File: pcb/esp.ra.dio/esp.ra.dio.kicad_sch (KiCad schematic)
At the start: 20 parts, among them J1 A, J2 B, J3 C, J4 D, J5 START, J6 SELECT, J7 JOY, J8 BATTERY, J9 NRF24L01 Connector, SW1 OPTS, SW2 POWER, U1 RP2040 Tiny, U3 MIC5205-3.0YM5

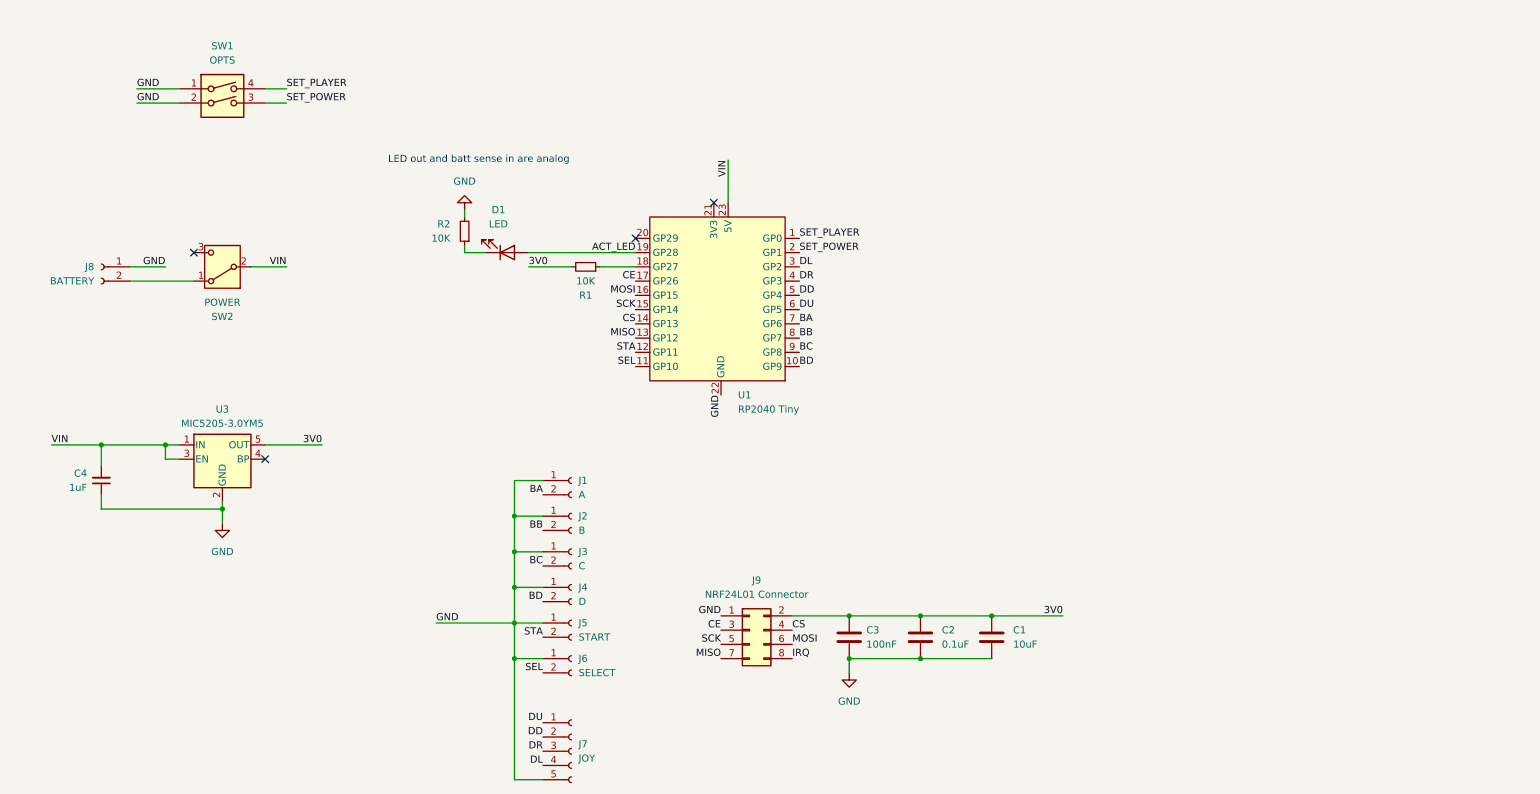
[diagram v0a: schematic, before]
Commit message: super-mini symbol/footprint
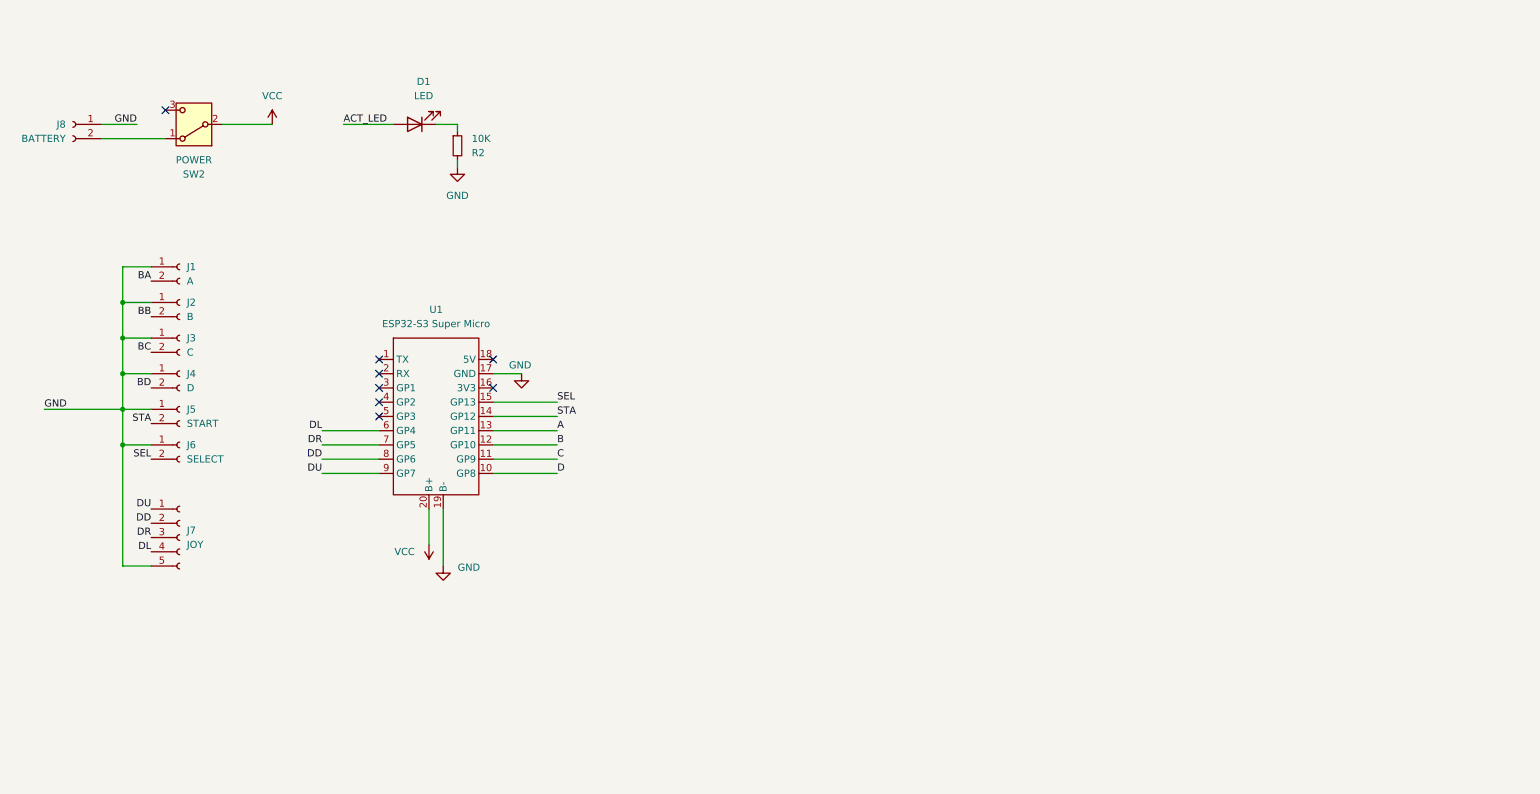
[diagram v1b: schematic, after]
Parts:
- removed C1: 10uF, Capacitor_SMD:C_0805_2012Metric_Pad1.18x1.45mm_HandSolder, symbol Device:C
- removed C2: 0.1uF, Capacitor_SMD:C_0805_2012Metric_Pad1.18x1.45mm_HandSolder, symbol Device:C
- removed C3: 100nF, Capacitor_SMD:C_0805_2012Metric_Pad1.18x1.45mm_HandSolder, symbol Device:C
- removed C4: 1uF, Capacitor_SMD:C_0805_2012Metric_Pad1.18x1.45mm_HandSolder, symbol Device:C_Small
- removed J9: NRF24L01 Connector, Connector_PinHeader_2.54mm:PinHeader_2x04_P2.54mm_Vertical, symbol Connector_Generic:Conn_02x04_Odd_Even
- removed R1: 10K, Resistor_SMD:R_0805_2012Metric_Pad1.20x1.40mm_HandSolder, symbol Device:R_Small
- removed SW1: OPTS, Button_Switch_SMD:SW_DIP_SPSTx02_Slide_6.7x6.64mm_W8.61mm_P2.54mm_LowProfile, symbol Switch:SW_DIP_x02
- removed U1: RP2040 Tiny, RP2040Zero:RP2040-Zero, symbol RP2040Zero:RP2040-Zero
- removed U3: MIC5205-3.0YM5, Package_TO_SOT_SMD:SOT-23-5, symbol Regulator_Linear:MIC5205-3.0YM5
- added U1: ESP32-S3 Super Micro, MCU_Espressif_ESP32_DevBoard:ESP32-S3-SuperMicro, symbol MCU_Espressif_ESP32_DevBoard:ESP32-S3-SuperMicro
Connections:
- net DD: now also U1.8 (GP6)
- net DL: now also U1.6 (GP4)
- net DR: now also U1.7 (GP5)
- net DU: now also U1.9 (GP7)
- net GND: now also U1.17 (GND), U1.19 (B-)
- net SEL: now also U1.15 (GP13)
- net STA: now also U1.14 (GP12)
- net VIN renamed VCC
- net VCC: now also U1.20 (B+)
- new net A: U1.13 (GP11)
- new net B: U1.12 (GP10)
- new net C: U1.11 (GP9)
- new net D: U1.10 (GP8)
- no-connect marks 4 -> 8
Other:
- note removed: "LED out and batt sense in are analog"
- moved on the sheet: D1, J1, J2, J3, J4, J5, J6, J7, J8, R2, SW2

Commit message: .
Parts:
- removed D1: LED, LED_THT:LED_D3.0mm_Horizontal_O1.27mm_Z6.0mm, symbol Device:LED
- removed R2: 10K, Resistor_SMD:R_0805_2012Metric_Pad1.20x1.40mm_HandSolder, symbol Device:R_Small
- removed SW2: POWER, Button_Switch_THT:SW_Slide_SPDT_Angled_CK_OS102011MA1Q, symbol Switch:SW_SPDT
- J8: value BATTERY -> BAT
- U1: footprint MCU_Espressif_ESP32_DevBoard:ESP32-S3-SuperMicro -> MCU_Espressif_ESP32_DevBoard:ESP32-S3-SuperMicro_SMD_BATT
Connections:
- net A is gone; now on net BA: U1.13 (GP11)
- net B is gone; now on net BB: U1.12 (GP10)
- net C is gone; now on net BC: U1.11 (GP9)
- net D is gone; now on net BD: U1.10 (GP8)
- net VCC is gone; now on net B+: U1.20 (B+)
- net B+: now reaches J8.2 (Pin_2)
- no-connect marks 8 -> 7
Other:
- moved on the sheet: J8

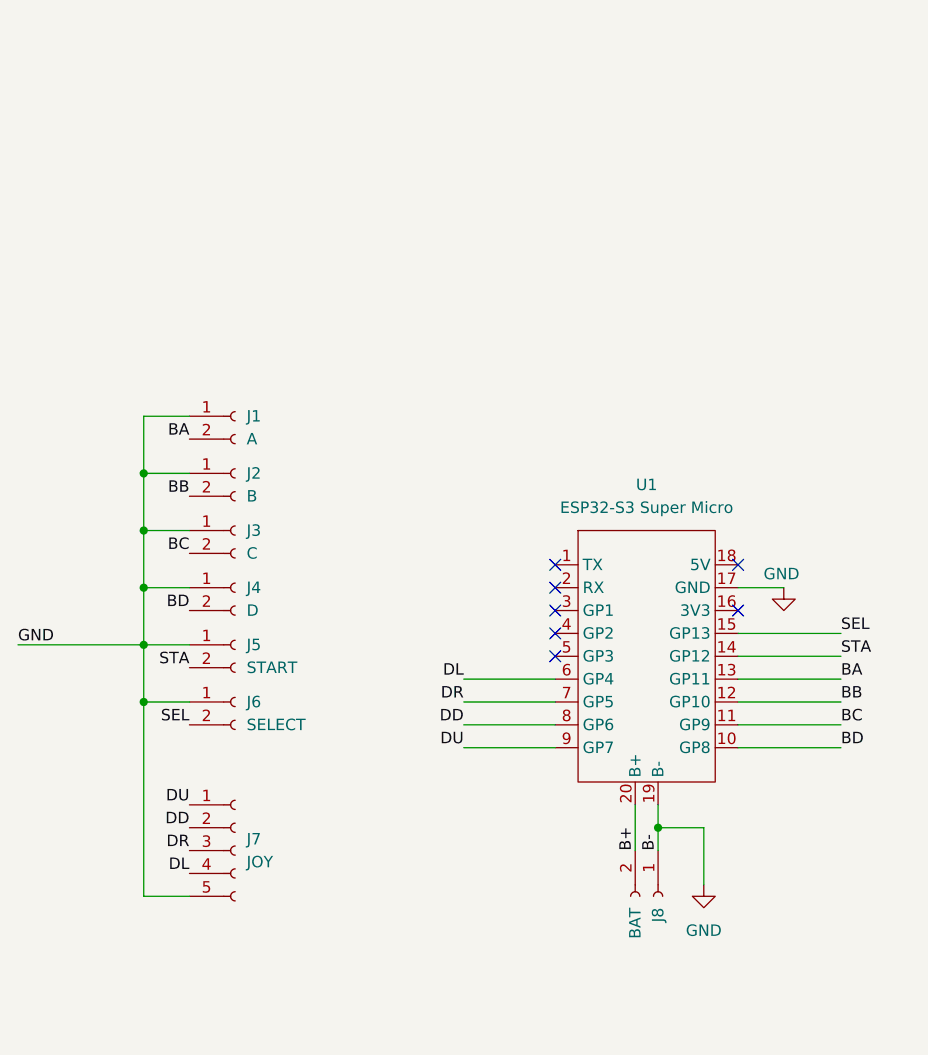
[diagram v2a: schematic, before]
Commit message: Updated layout that keeps LED and switch
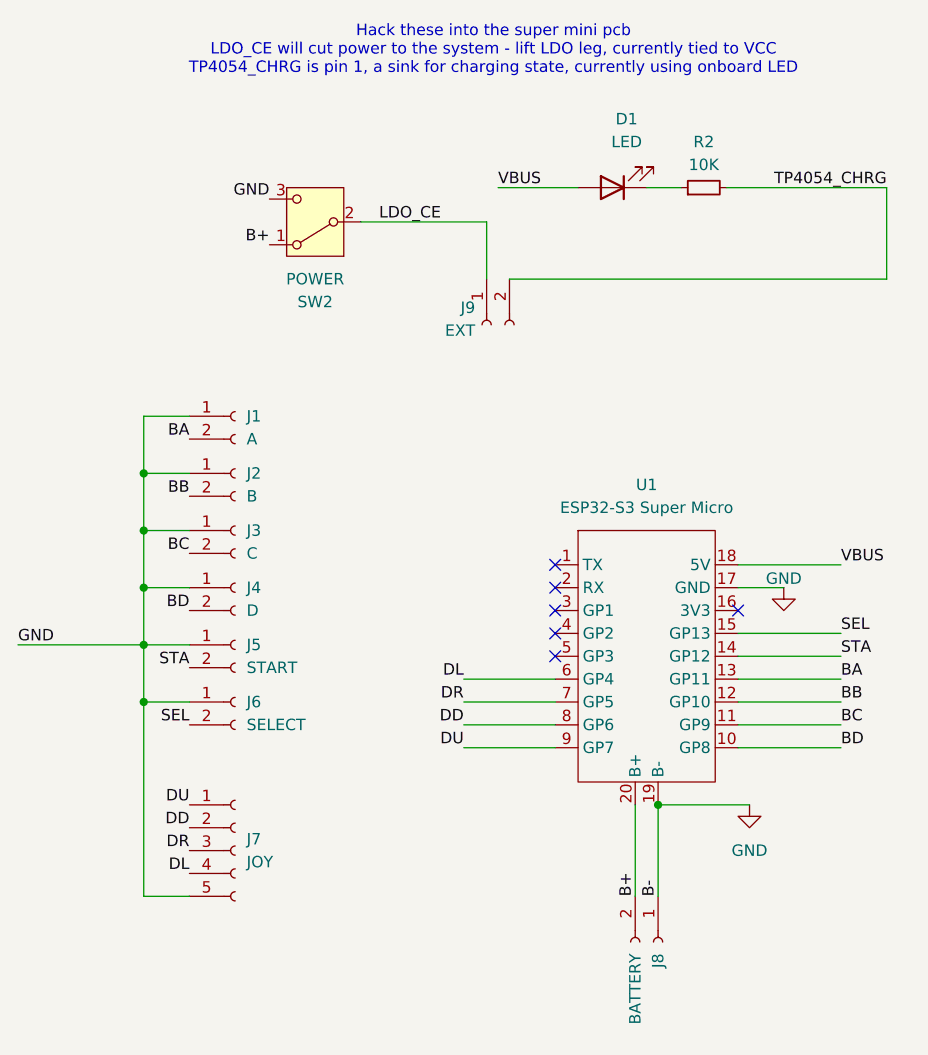
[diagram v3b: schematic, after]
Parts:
- added D1: LED, LED_THT:LED_D3.0mm_Horizontal_O1.27mm_Z6.0mm, symbol Device:LED
- added J9: EXT, Connector_PinHeader_2.54mm:PinHeader_1x02_P2.54mm_Vertical, symbol Connector:Conn_01x02_Socket
- added R2: 10K, Resistor_SMD:R_0805_2012Metric_Pad1.20x1.40mm_HandSolder, symbol Device:R_Small
- added SW2: POWER, Button_Switch_THT:SW_Slide_SPDT_Angled_CK_OS102011MA1Q, symbol Switch:SW_SPDT
- J8: value BAT -> BATTERY
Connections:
- net B+: now also SW2.1 (A)
- net GND: now also SW2.3 (C)
- net VBUS: now reaches U1.18 (5V)
- net VBUS: now also D1.2 (A)
- new net: D1.1 (K), R2.1
- new net LDO_CE: J9.1 (Pin_1), SW2.2 (B)
- new net TP4054_CHRG: J9.2 (Pin_2), R2.2
- no-connect marks 7 -> 6
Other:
- note added: "Hack these into the super mini pcb LDO_CE will cut power to the system - lift LDO leg, currently tied to VCC TP4054_CHRG is pin 1, a sink for charging state, currently using onboard LED"
- moved on the sheet: J8

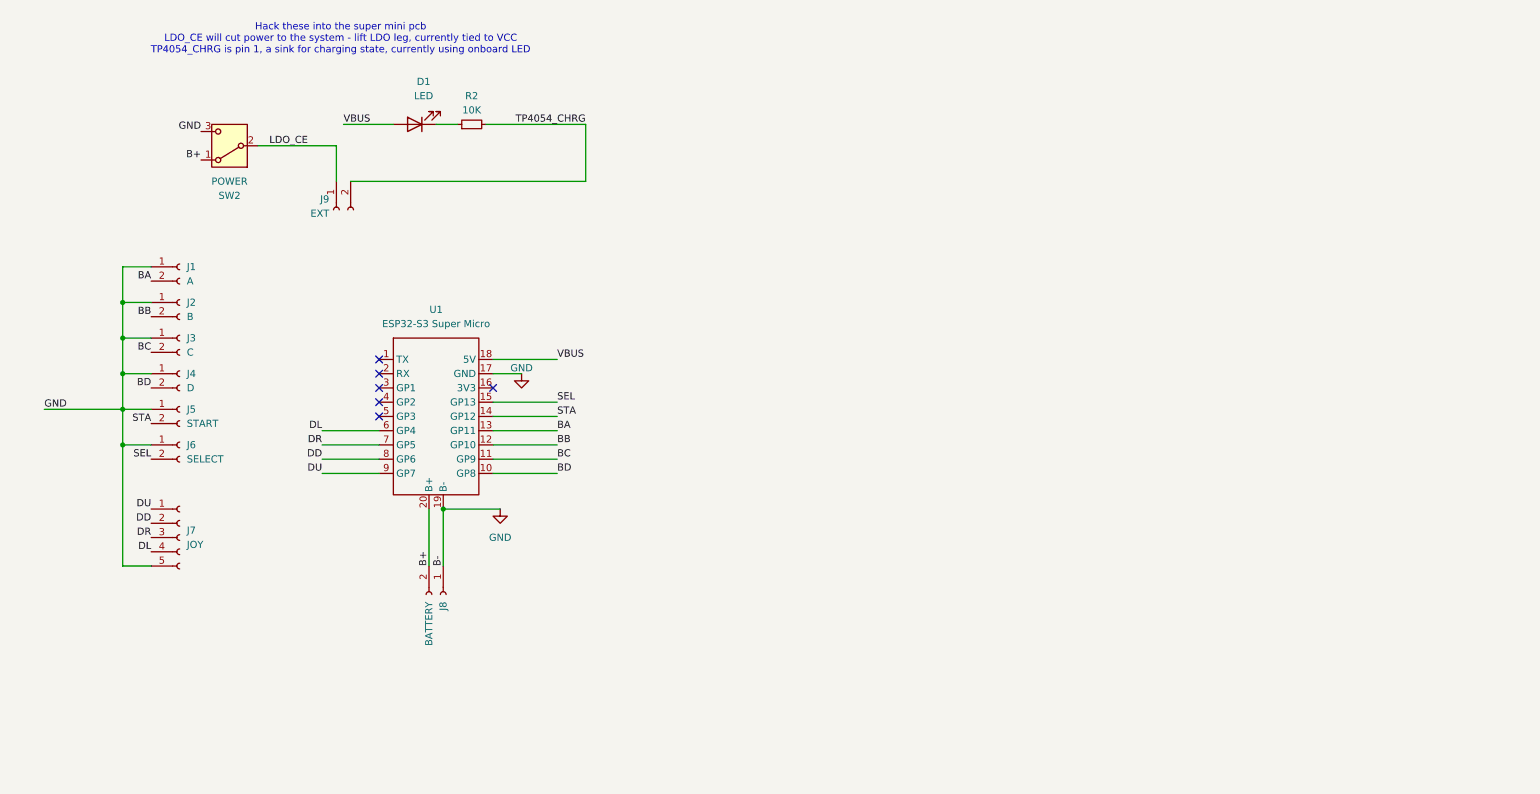
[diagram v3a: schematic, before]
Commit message: Enough dev boards, redo with WROOM
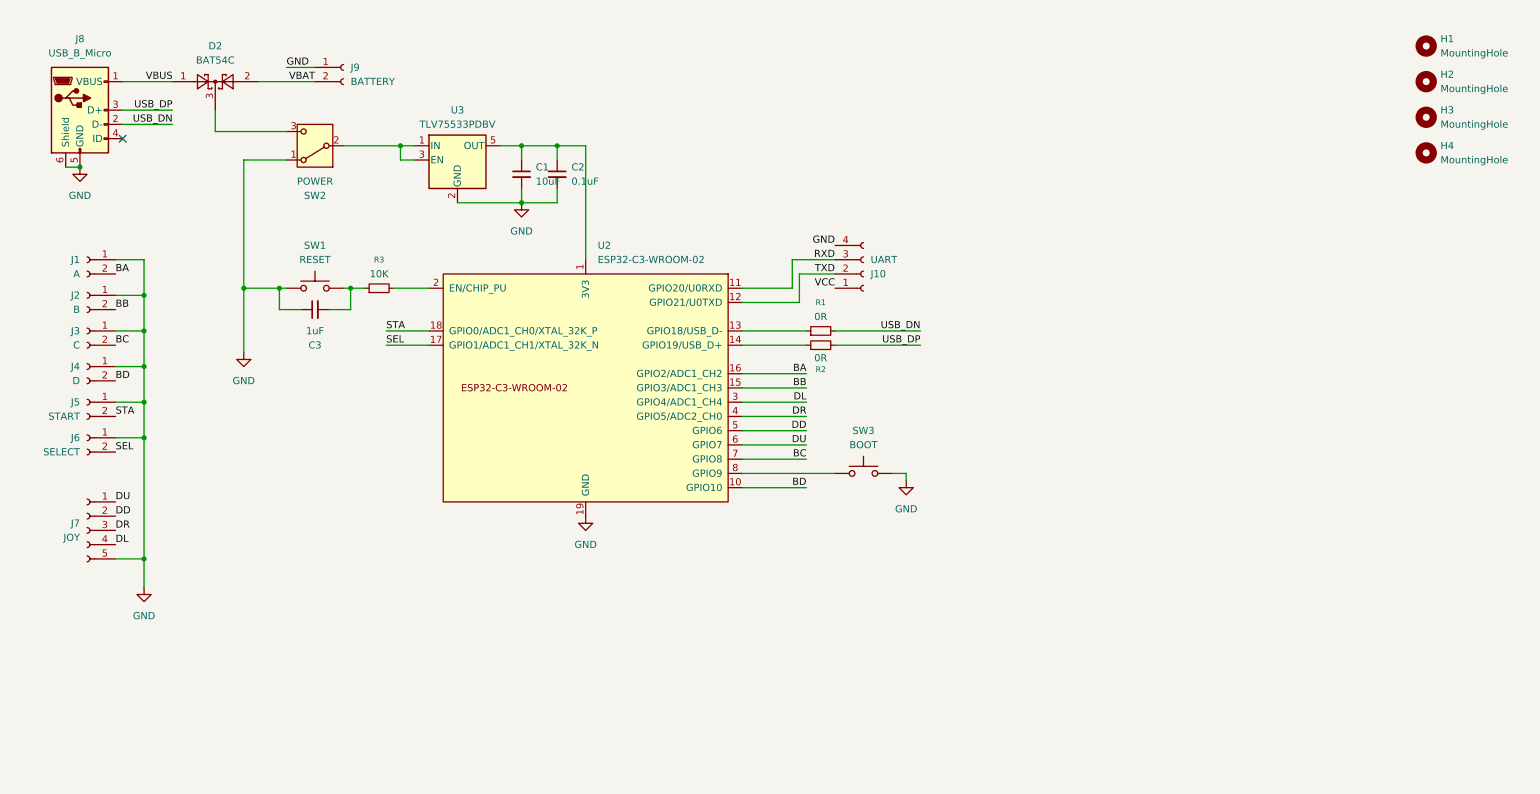
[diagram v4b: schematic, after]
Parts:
- removed D1: LED, LED_THT:LED_D3.0mm_Horizontal_O1.27mm_Z6.0mm, symbol Device:LED
- removed J8: BATTERY, Connector_JST:JST_PH_B2B-PH-K_1x02_P2.00mm_Vertical, symbol Connector:Conn_01x02_Socket
- removed U1: ESP32-S3 Super Micro, MCU_Espressif_ESP32_DevBoard:ESP32-S3-SuperMicro_SMD_BATT, symbol MCU_Espressif_ESP32_DevBoard:ESP32-S3-SuperMicro
- added C1: 10uF, symbol Device:C_Small
- added C2: 0.1uF, symbol Device:C_Small
- added C3: 1uF, symbol Device:C_Small
- added D2: BAT54C, Package_TO_SOT_SMD:SOT-23, symbol Diode:BAT54C
- added H1, H2, H3, H4: MountingHole, symbol Mechanical:MountingHole
- added J10: UART, symbol Connector:Conn_01x04_Socket
- added J8: USB_B_Micro, Connector_USB:USB_Micro-B_Amphenol_10118193-0001LF_Horizontal, symbol Connector:USB_B_Micro
- added R1: 0R, symbol Device:R_Small
- added R3: 10K, symbol Device:R_Small
- added SW1: RESET, symbol Switch:SW_Push
- added SW3: BOOT, symbol Switch:SW_Push
- added U2: ESP32-C3-WROOM-02, PCM_Espressif:ESP32-C3-WROOM-02, symbol PCM_Espressif:ESP32-C3-WROOM-02
- added U3: TLV75533PDBV, Package_TO_SOT_SMD:SOT-23-5, symbol Regulator_Linear:TLV75533PDBV
- J9: value EXT -> BATTERY; footprint Connector_PinHeader_2.54mm:PinHeader_1x02_P2.54mm_Vertical -> Connector_JST:JST_PH_B2B-PH-K_1x02_P2.00mm_Vertical
- R2: value 10K -> 0R; footprint Resistor_SMD:R_0805_2012Metric_Pad1.20x1.40mm_HandSolder -> (none)
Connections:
- net B+ is gone; now on net GND: SW2.1 (A)
- net BA: now also U2.16 (GPIO2/ADC1_CH2)
- net BB: now also U2.15 (GPIO3/ADC1_CH3)
- net BC: now also U2.7 (GPIO8)
- net BD: now also U2.10 (GPIO10)
- net DD: now also U2.5 (GPIO6)
- net DL: now also U2.3 (GPIO4/ADC1_CH4)
- net DR: now also U2.4 (GPIO5/ADC2_CH0)
- net DU: now also U2.6 (GPIO7)
- net GND: now also J9.1 (Pin_1), C1.2, C2.2, C3.1, J10.4 (Pin_4), J8.5 (GND), J8.6 (Shield), SW1.1, SW3.2, U2.19 (GND), U2.9 (GND), U3.2 (GND); no longer SW2.3 (C)
- net SEL: now also U2.17 (GPIO1/ADC1_CH1/XTAL_32K_N)
- net STA: now also U2.18 (GPIO0/ADC1_CH0/XTAL_32K_P)
- net VBUS: now also D2.1, J8.1 (VBUS)
- net at R2.1: now also U2.14 (GPIO19/USB_D+)
- net LDO_CE: no longer names the net of SW2.2 (B)
- net LDO_CE: now also U3.1 (IN), U3.3 (EN); no longer J9.1 (Pin_1)
- net TP4054_CHRG renamed USB_DP
- net USB_DP: now also J8.3 (D+); no longer J9.2 (Pin_2)
- new net: C1.1, C2.1, U2.1 (3V3), U3.5 (OUT)
- new net: C3.2, R3.1, SW1.2
- new net: R1.1, U2.13 (GPIO18/USB_D-)
- new net: R3.2, U2.2 (EN/CHIP_PU)
- new net: SW3.1, U2.8 (GPIO9)
- new net: D2.3, SW2.3 (C)
- new net RXD: J10.3 (Pin_3), U2.11 (GPIO20/U0RXD)
- new net TXD: J10.2 (Pin_2), U2.12 (GPIO21/U0TXD)
- new net USB_DN: J8.2 (D-), R1.2
- new net VBAT: D2.2, J9.2 (Pin_2)
- new net VCC: J10.1 (Pin_1)
- no-connect marks 6 -> 1
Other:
- note removed: "Hack these into the super mini pcb LDO_CE will cut power to the system - lift LDO leg, currently tied to VCC TP4054_CHRG is pin 1, a sink for charging state, currently using onboard LED"
- moved on the sheet: J1, J2, J3, J4, J5, J6, J7, SW2
